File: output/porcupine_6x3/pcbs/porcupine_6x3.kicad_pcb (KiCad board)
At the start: 2 copper layers, 166.4 x 113.7 mm, 60 parts, among them J1 Jumper, J2 Jumper

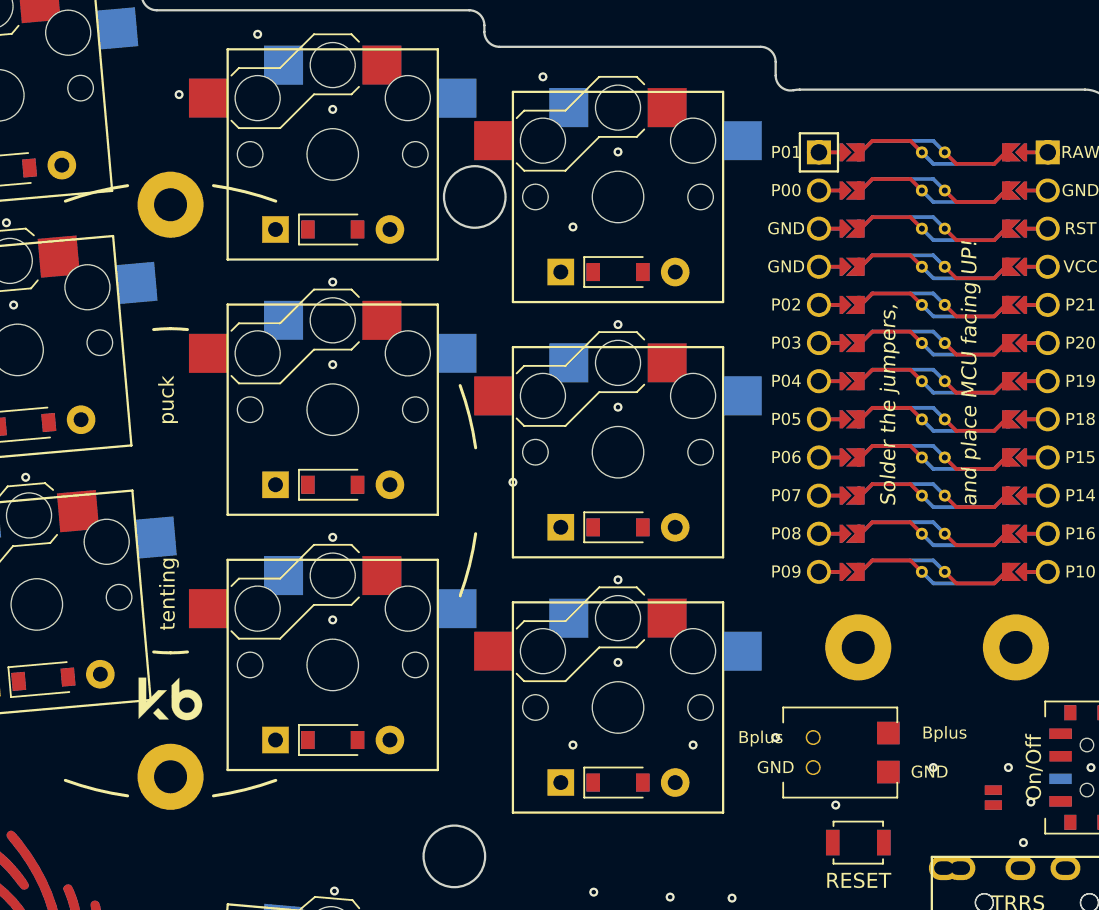
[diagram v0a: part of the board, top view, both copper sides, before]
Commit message: Update input and add manually routed boards
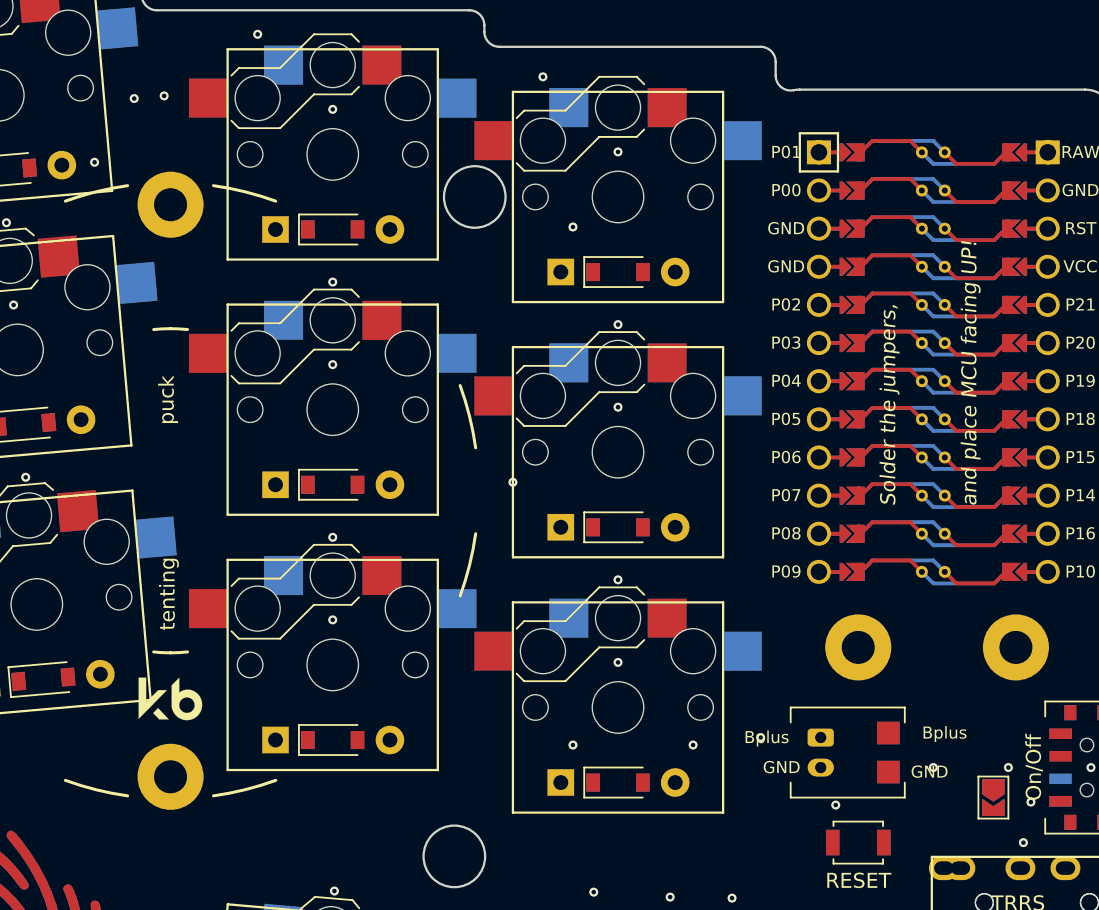
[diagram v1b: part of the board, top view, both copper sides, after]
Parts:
- removed _79, _80: hole, Through Hole
- added _81: hole, Through Hole, F.Cu at (260.5, 133.1)
- added _82: hole, Through Hole, F.Cu at (271.0, 133.1)
- D1, D10, D11, D12, D13, D14, D15, D16, D17, D18, D19, D2, D20, D21, D3, D4, D5, D6, D7, D8, D9: footprint Diode_SMD:D_SOD-123 -> Diode_SMD:SOD-123
- J1: footprint PCM12SMTR -> Jumper:SolderJumper-2_P1.3mm_Open_TrianglePad1.0x1.5mm; moved to B.Cu
- J2: footprint PCM12SMTR -> Jumper:SolderJumper-2_P1.3mm_Open_TrianglePad1.0x1.5mm
- moved _2 0.50 mm to (258.0, 140.1)
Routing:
- net outer_top: vias 1 -> 0
- net outer_bottom: vias 0 -> 1
- net P20: vias 3 -> 5
- net P15: vias 5 -> 6
- net P14: vias 5 -> 4

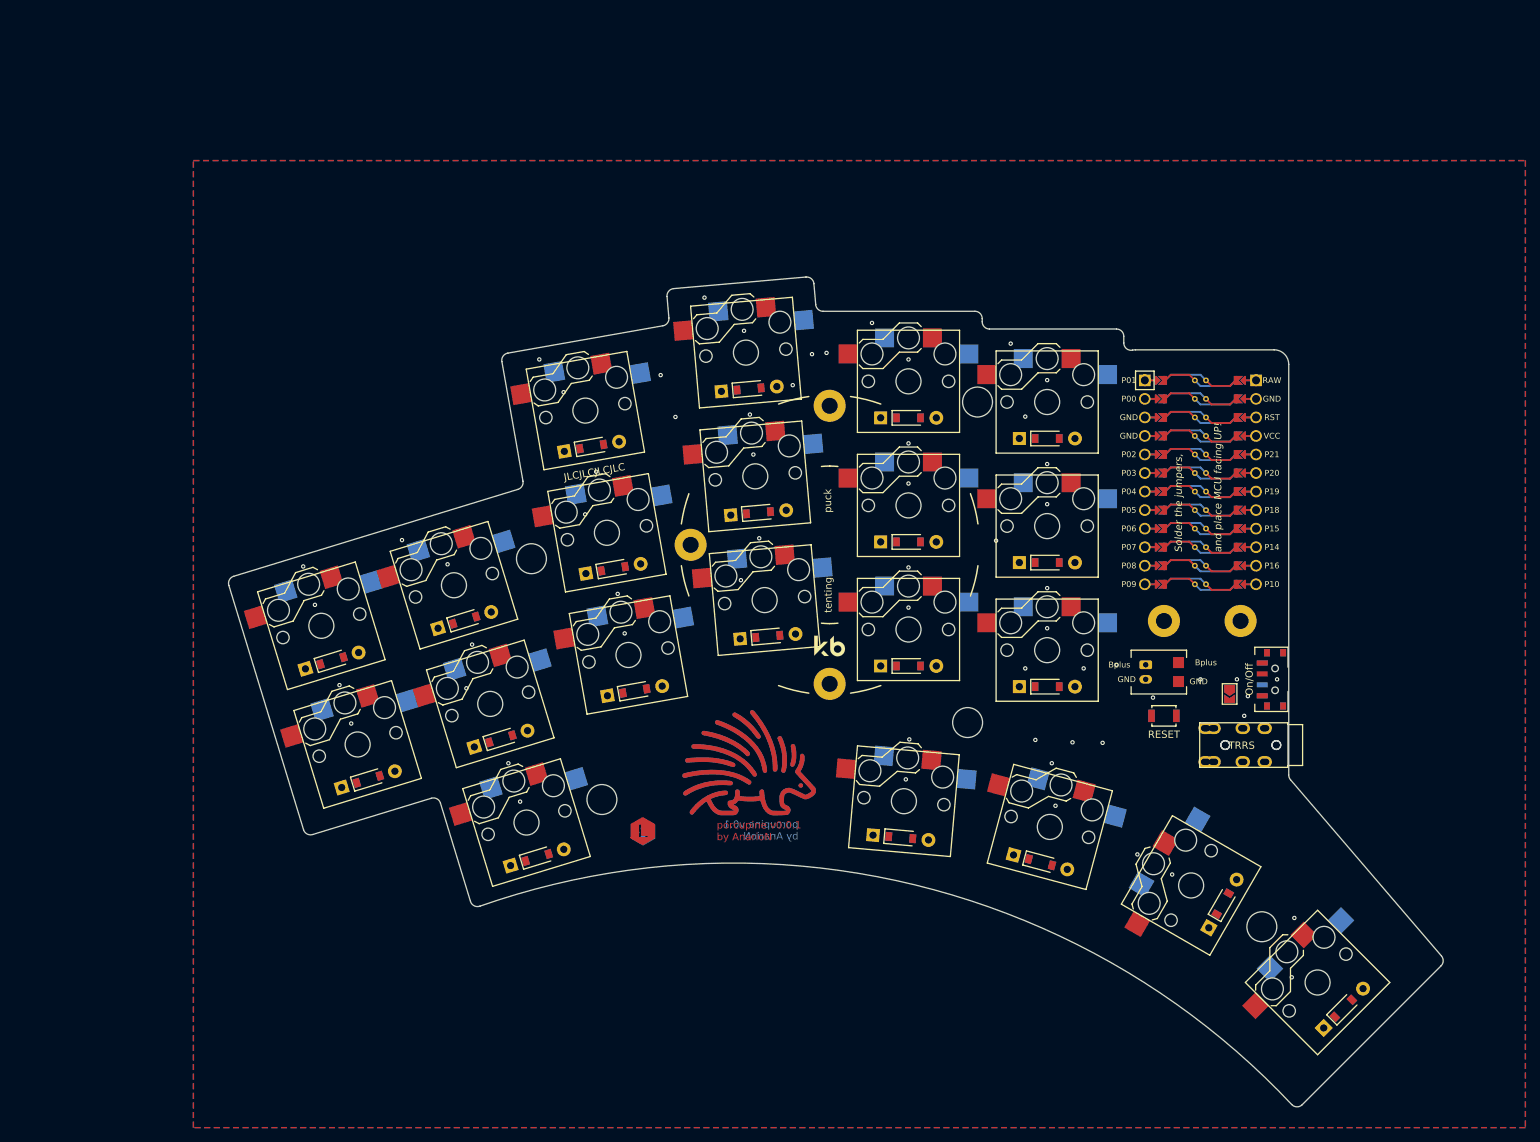
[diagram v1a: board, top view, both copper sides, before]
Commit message: Update 6x3 variant
* Removed unnecessary P19 via
* Fix outer column stagger
* Fix P19 matrix ring bottom via
* Resized GND zones
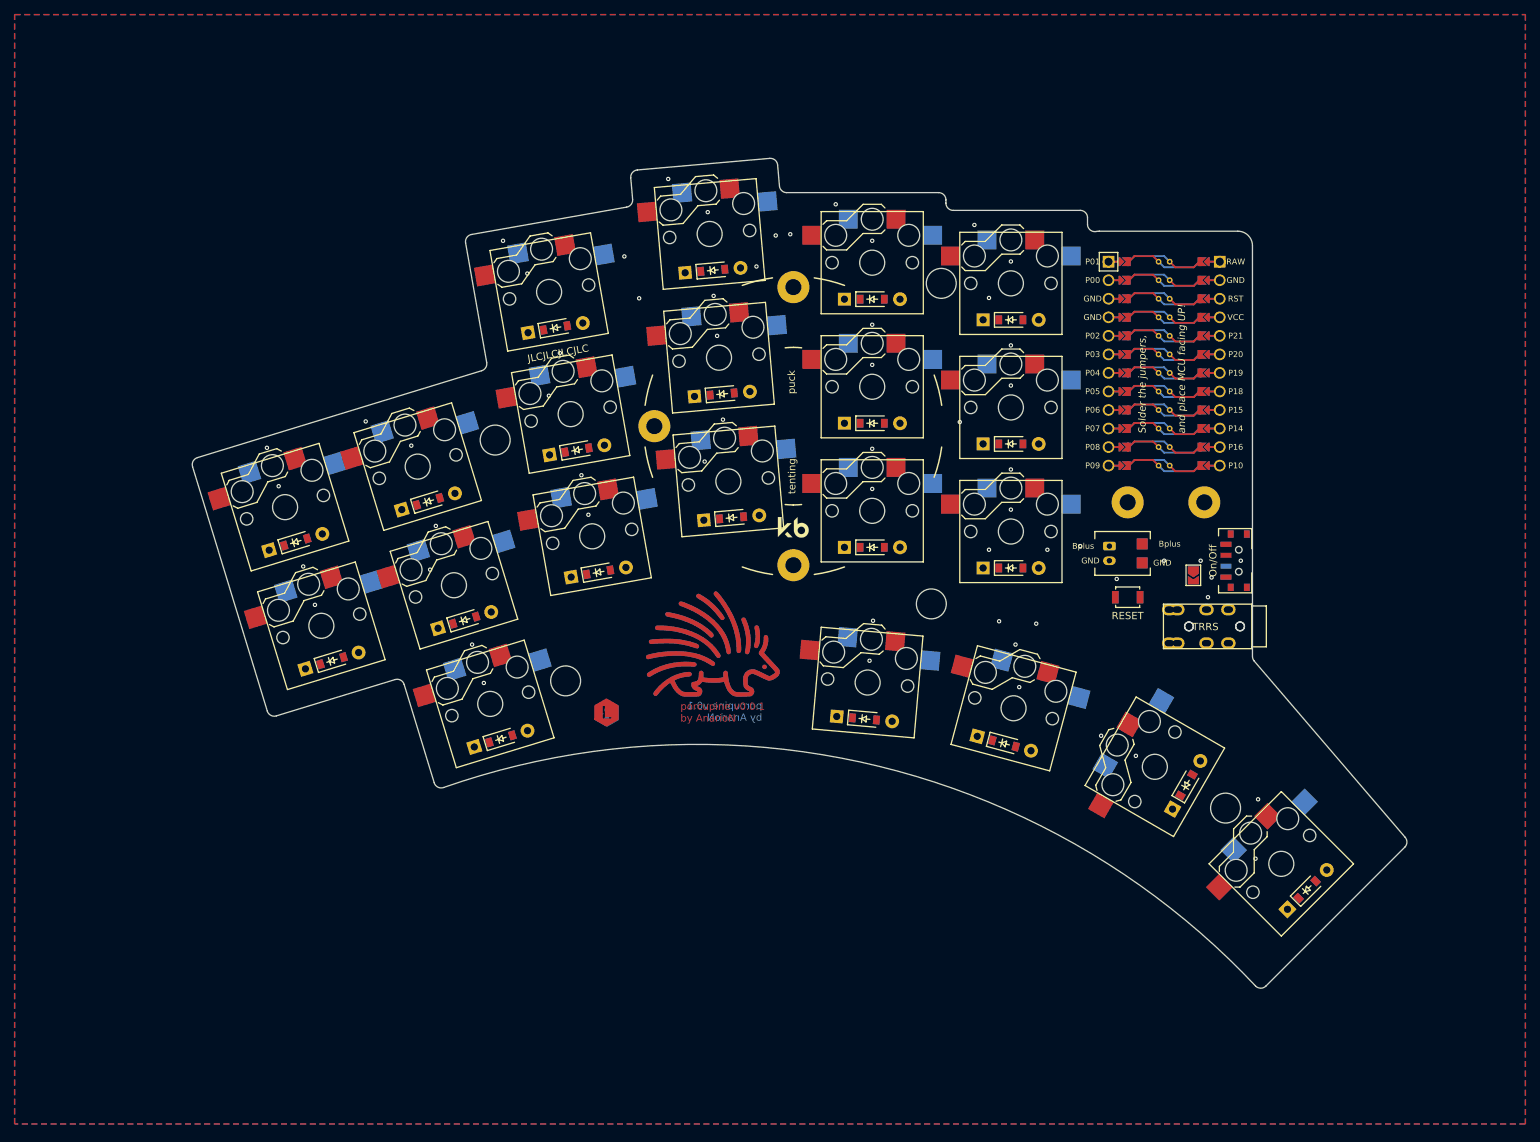
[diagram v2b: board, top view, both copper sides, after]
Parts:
- removed _82: hole, Through Hole
- added _80: hole, Through Hole, F.Cu at (255.5, 116.8)
- moved _81 17.2 mm to (266.0, 116.8)
- moved D6 17.0 mm to (183.0, 126.4)
- moved D7 17.0 mm to (180.1, 109.7)
- moved D8 17.0 mm to (177.1, 92.9)
- moved S6 17.0 mm to (182.1, 121.5)
- moved S7 17.0 mm to (179.2, 104.7)
- moved S8 17.0 mm to (176.2, 88.0)
- moved D1 17.0 mm to (146.5, 138.5)
- moved D10 17.0 mm to (200.0, 102.0)
- moved D11 17.0 mm to (198.7, 85.0)
- moved D2 17.0 mm to (141.5, 122.3)
- moved S1 17.0 mm to (145.0, 133.7)
- moved S10 17.0 mm to (199.5, 97.0)
- moved S11 17.0 mm to (198.2, 80.1)
- moved S2 17.0 mm to (140.1, 117.5)
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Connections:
- D1 pad 1: outer_bottom -> outer_home
- D1 pad 2: P6 -> P5
- D2 pad 1: outer_home -> outer_top
- D2 pad 2: P5 -> P4
- S1 pad 1: outer_bottom -> outer_home
- S2 pad 1: outer_home -> outer_top
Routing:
- net outer_top: vias 0 -> 1
- net outer_bottom: vias 1 -> 0
- net P15: vias 6 -> 5

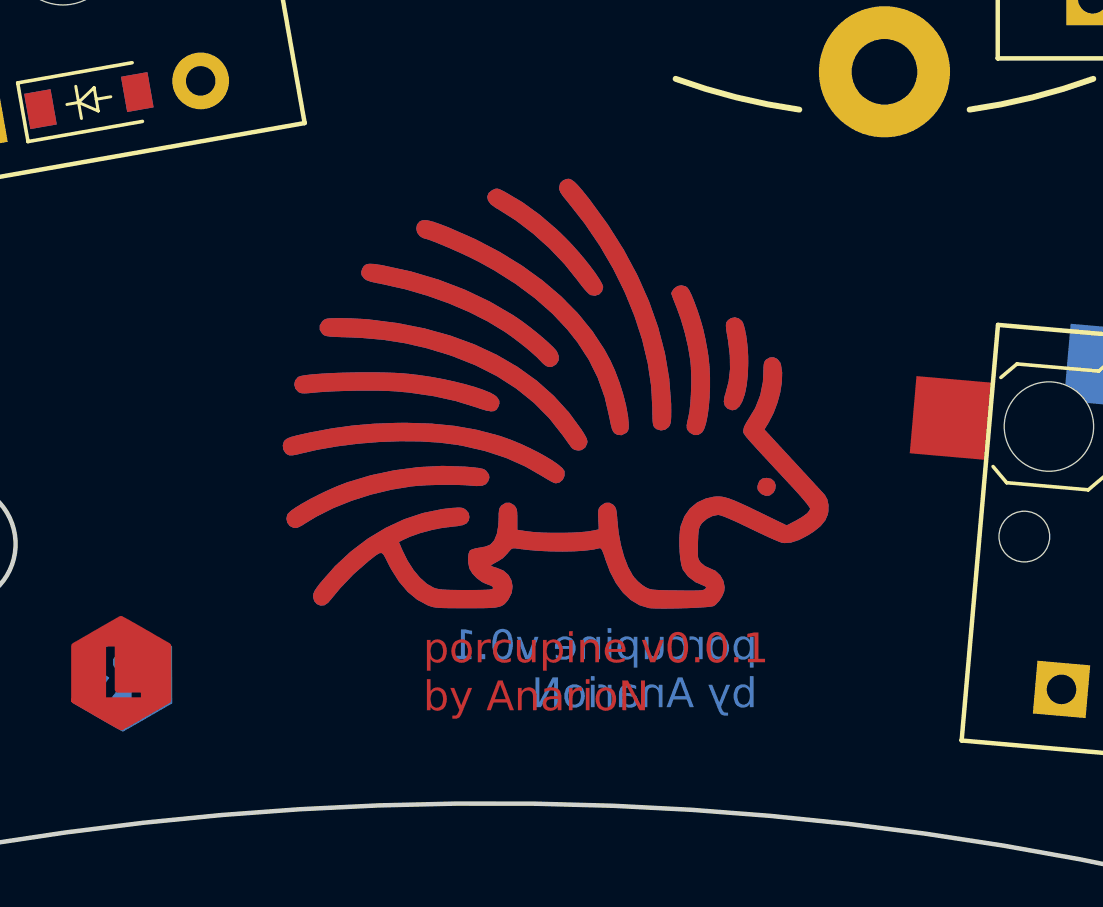
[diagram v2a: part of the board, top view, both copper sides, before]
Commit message: Add new logo
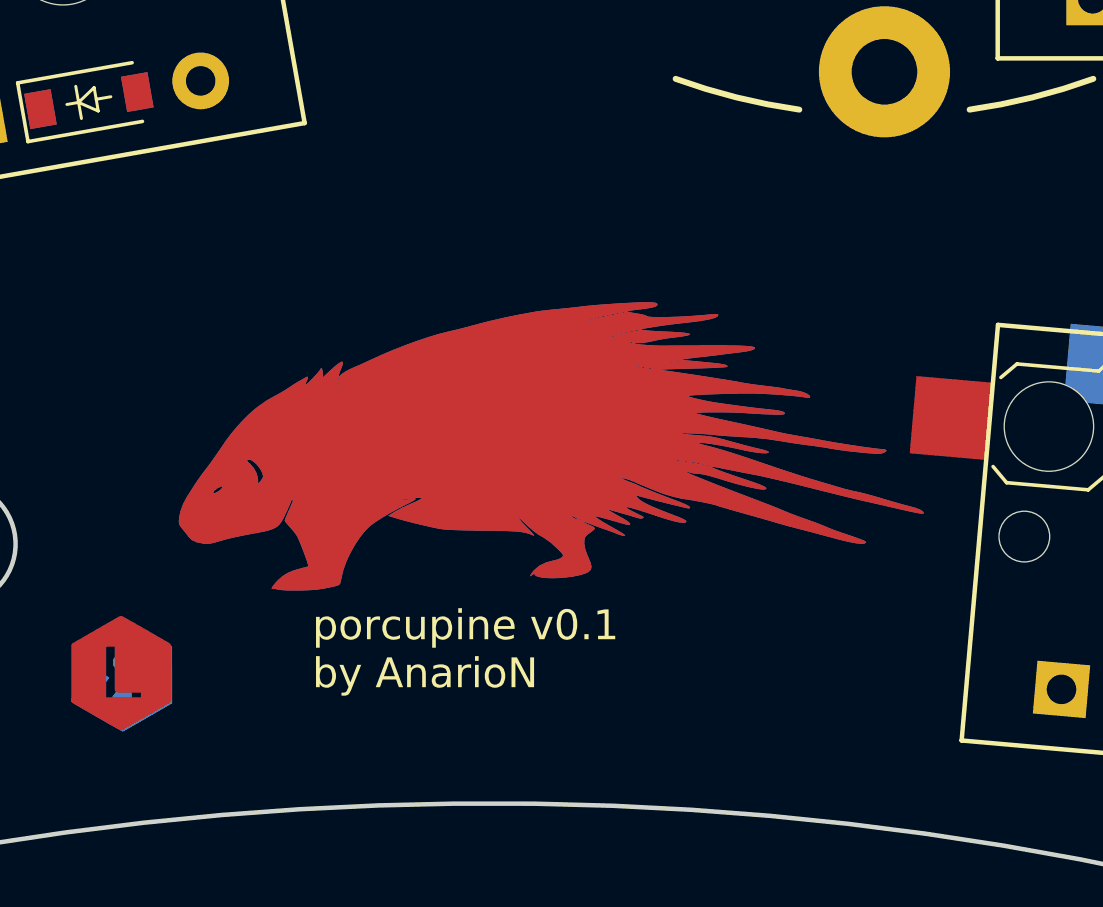
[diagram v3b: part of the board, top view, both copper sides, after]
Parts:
- removed _11: Tenting Puck, Tenting Puck
- removed _80, _81: hole, Through Hole
- added _78: hole, Through Hole, F.Cu at (255.5, 116.8)
- added _79: hole, Through Hole, F.Cu at (266.0, 116.8)
- added _9: Tenting Puck, Tenting Puck, F.Cu at (209.7, 106.4)
- moved LOGO_B 1.75 mm to (198.5, 138.0)
- moved LOGO_F 1.75 mm to (198.5, 138.0)
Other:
- board text removed: "porcupine v0.0.1 by AnarioN"
